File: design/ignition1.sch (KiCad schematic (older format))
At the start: 9 parts, among them P16 CONN_1, P17 CONN_1, Q6 MOSFET_N, SW6 SWITCH_INV

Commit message: new ignition circuit, new usb-serial IC WARNING: The FT232RL doesnt support 125deg C
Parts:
- removed R36: 1k, R4-SM0805, symbol R
- removed SW6: SWITCH_INV, SIL-3, symbol SWITCH_INV
- added D?: DIODE, symbol DIODE
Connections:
- net labels removed: 5V_reg
- wire segments 15 -> 13
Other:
- note added: "coil will be always at 12v..."
- moved on the sheet: P16, P17
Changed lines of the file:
@@
-EESchema Schematic File Version 2  date Fri 06 Aug 2010 10:16:31 PM ART
+EESchema Schematic File Version 2  date Sun 15 Aug 2010 12:57:33 PM ART
 LIBS:power
 LIBS:freeEMS_lib
@@
 EELAYER END
 $Descr A4 11700 8267
-Sheet 21 48
+Sheet 29 48
 Title "freeEMS 1.0"
-Date "7 aug 2010"
+Date "15 aug 2010"
 Rev "A.07"
 Comp "diyefi.org"
@@
 Comment4 ""
 $EndDescr
-Connection ~ 3400 2650
 Wire Wire Line
-	3400 2550 3400 2650
+	4300 2250 4100 2250
+Connection ~ 4100 1750
 Wire Wire Line
-	1750 1350 1950 1350
+	4200 1750 4100 1750
 Wire Wire Line
-	3050 1650 3050 1450
-Connection ~ 4100 1450
+	4100 1650 4100 1850
 Wire Wire Line
-	3550 1450 5100 1450
+	4100 1650 4050 1650
+Connection ~ 3050 1450
+Connection ~ 3400 2050
 Wire Wire Line
-	5100 1450 5100 2200
+	3550 1650 3650 1650
 Wire Wire Line
-	5100 2200 5300 2200
+	2750 2650 4100 2650
 Wire Wire Line
-	4100 1450 4100 1850
+	3800 2050 3350 2050
 Wire Wire Line
-	3050 1450 2950 1450
+	2800 2050 2850 2050
 Wire Wire Line
 	4100 2650 4100 2250
 Wire Wire Line
-	2800 2050 2850 2050
+	3050 1650 3050 1450
 Wire Wire Line
-	3800 2050 3350 2050
+	3400 2650 3400 2550
+Connection ~ 3400 2650
 Wire Wire Line
-	2750 2650 5300 2650
-Connection ~ 4100 2650
+	2950 1450 4200 1450
 Wire Wire Line
-	4050 1650 4100 1650
-Connection ~ 4100 1650
-Wire Wire Line
-	3550 1650 3650 1650
-Wire Wire Line
-	1750 1550 1950 1550
-Connection ~ 3400 2050
+	4100 1850 4300 1850
+$Comp
+L DIODE D?
+U 1 1 4C66EF49
+P 4300 2050
+F 0 "D?" H 4300 2150 40  0000 C CNN
+F 1 "DIODE" H 4300 1950 40  0000 C CNN
+	1    4300 2050
+	0    -1   -1   0
+$EndComp
+Text Notes 1850 3500 0    60   ~ 0
+coil will be always at 12v...
 $Comp
 L PIP-3104 Q6
@@
 	1    3400 2300
 	-1   0    0    1
-$EndComp
-$Comp
-L SWITCH_INV SW6
-U 1 1 48AE0832
-P 2450 1450
-F 0 "SW6" H 2250 1600 50  0000 C CNN
-F 1 "SWITCH_INV" H 2300 1300 50  0000 C CNN
-F 2 "SIL-3" H 2350 1700 60  0001 C CNN
-	1    2450 1450
-	-1   0    0    -1
 $EndComp
 $Comp
@@
 L CONN_1 P17
 U 1 1 4C2F5317
-P 5450 2650
-F 0 "P17" H 5530 2650 40  0000 L CNN
-F 1 "CONN_1" H 5450 2705 30  0001 C CNN
-F 2 "1PIN" V 1880 2850 60  0001 C CNN
-	1    5450 2650
+P 4350 1750
+F 0 "P17" H 4430 1750 40  0000 L CNN
+F 1 "CONN_1" H 4350 1805 30  0001 C CNN
+F 2 "1PIN" V 780 1950 60  0001 C CNN
+	1    4350 1750
 	1    0    0    -1
 $EndComp
@@
 L CONN_1 P16
 U 1 1 4C2F530E
-P 5450 2200
-F 0 "P16" H 5530 2200 40  0000 L CNN
-F 1 "CONN_1" H 5450 2255 30  0001 C CNN
-F 2 "1PIN" V 1880 2600 60  0001 C CNN
-	1    5450 2200
+P 4350 1450
+F 0 "P16" H 4430 1450 40  0000 L CNN
+F 1 "CONN_1" H 4350 1505 30  0001 C CNN
+F 2 "1PIN" V 780 1850 60  0001 C CNN
+	1    4350 1450
 	1    0    0    -1
 $EndComp
-Text HLabel 1750 1550 0    60   Input ~ 0
-5V_reg
 $Comp
 L R R35
@@
 	0    1    1    0
 $EndComp
-$Comp
-L R R36
-U 1 1 4C2F52E2
-P 3300 1450
-F 0 "R36" V 3380 1450 50  0000 C CNN
-F 1 "1k" V 3300 1450 50  0000 C CNN
-F 2 "R4-SM0805" V 3480 1550 60  0001 C CNN
-F 4 "newark,38k0327" V 1130 2350 60  0001 C CNN "Field1"
-F 5 "vendor1, smd w hem" V 1130 2350 60  0001 C CNN "Field2"
-F 6 "vendor2, thru w hem" V 1130 2350 60  0001 C CNN "Field3"
-F 7 "vendor2, smd w hem" V 1130 2350 60  0001 C CNN "Field4"
-F 8 "250,mW" V 1130 2350 60  0001 C CNN "Field5"
-F 9 "5,%" V 1130 2350 60  0001 C CNN "Field6"
-F 10 "carbon film" V 1130 2350 60  0001 C CNN "Field7"
-F 11 "other,more,stuff" V 1130 2350 60  0001 C CNN "Field8"
-	1    3300 1450
-	0    1    1    0
-$EndComp
-Text HLabel 1750 1350 0    60   Input ~ 0
+Text HLabel 2950 1450 0    60   Input ~ 0
 12V_bat
 Text HLabel 2750 2650 0    60   BiDi ~ 0

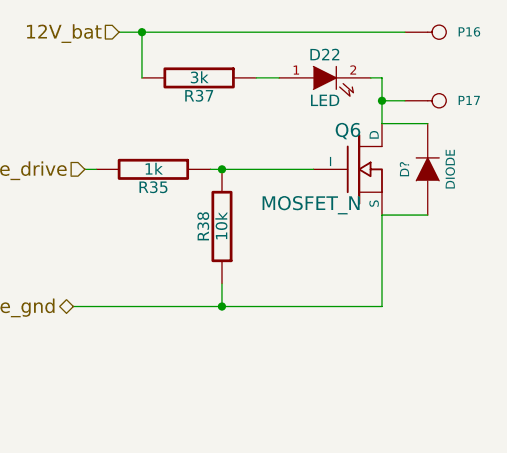
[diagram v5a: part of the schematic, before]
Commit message: now with 8 low Z injector drivers, BDM connector, FT232RL. 3 grounds: digital and analog, and power (isolated). I have to remove 2 ign drivers and rearrange the connector board pins.
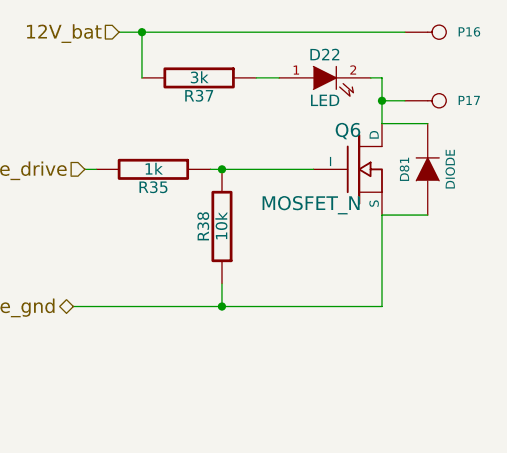
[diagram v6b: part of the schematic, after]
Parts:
- gave numbers to parts that had none: 1
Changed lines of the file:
@@
-EESchema Schematic File Version 2  date Sun 15 Aug 2010 12:57:33 PM ART
+EESchema Schematic File Version 2  date Sun 29 Aug 2010 06:27:37 AM ART
 LIBS:power
 LIBS:freeEMS_lib
@@
 EELAYER END
 $Descr A4 11700 8267
-Sheet 29 48
+Sheet 29 50
 Title "freeEMS 1.0"
-Date "15 aug 2010"
+Date "29 aug 2010"
 Rev "A.07"
 Comp "diyefi.org"
@@
 	4100 1850 4300 1850
 $Comp
-L DIODE D?
+L DIODE D81
 U 1 1 4C66EF49
 P 4300 2050
-F 0 "D?" H 4300 2150 40  0000 C CNN
+F 0 "D81" H 4300 2150 40  0000 C CNN
 F 1 "DIODE" H 4300 1950 40  0000 C CNN
 	1    4300 2050
